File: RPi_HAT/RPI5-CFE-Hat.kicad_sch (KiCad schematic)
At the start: 64 parts, among them J1 Conn_01x16_Shielded, J2 SFP, J3 Bus_M.2_Socket_M, J5 Conn_02x03_Odd_Even, Q1 DMG1012T, Q2 DMG1012T, Q3 DMG1012T, U1 TPS564242DRLR, U2 PCA9306, U3 LM1117MP-1.8

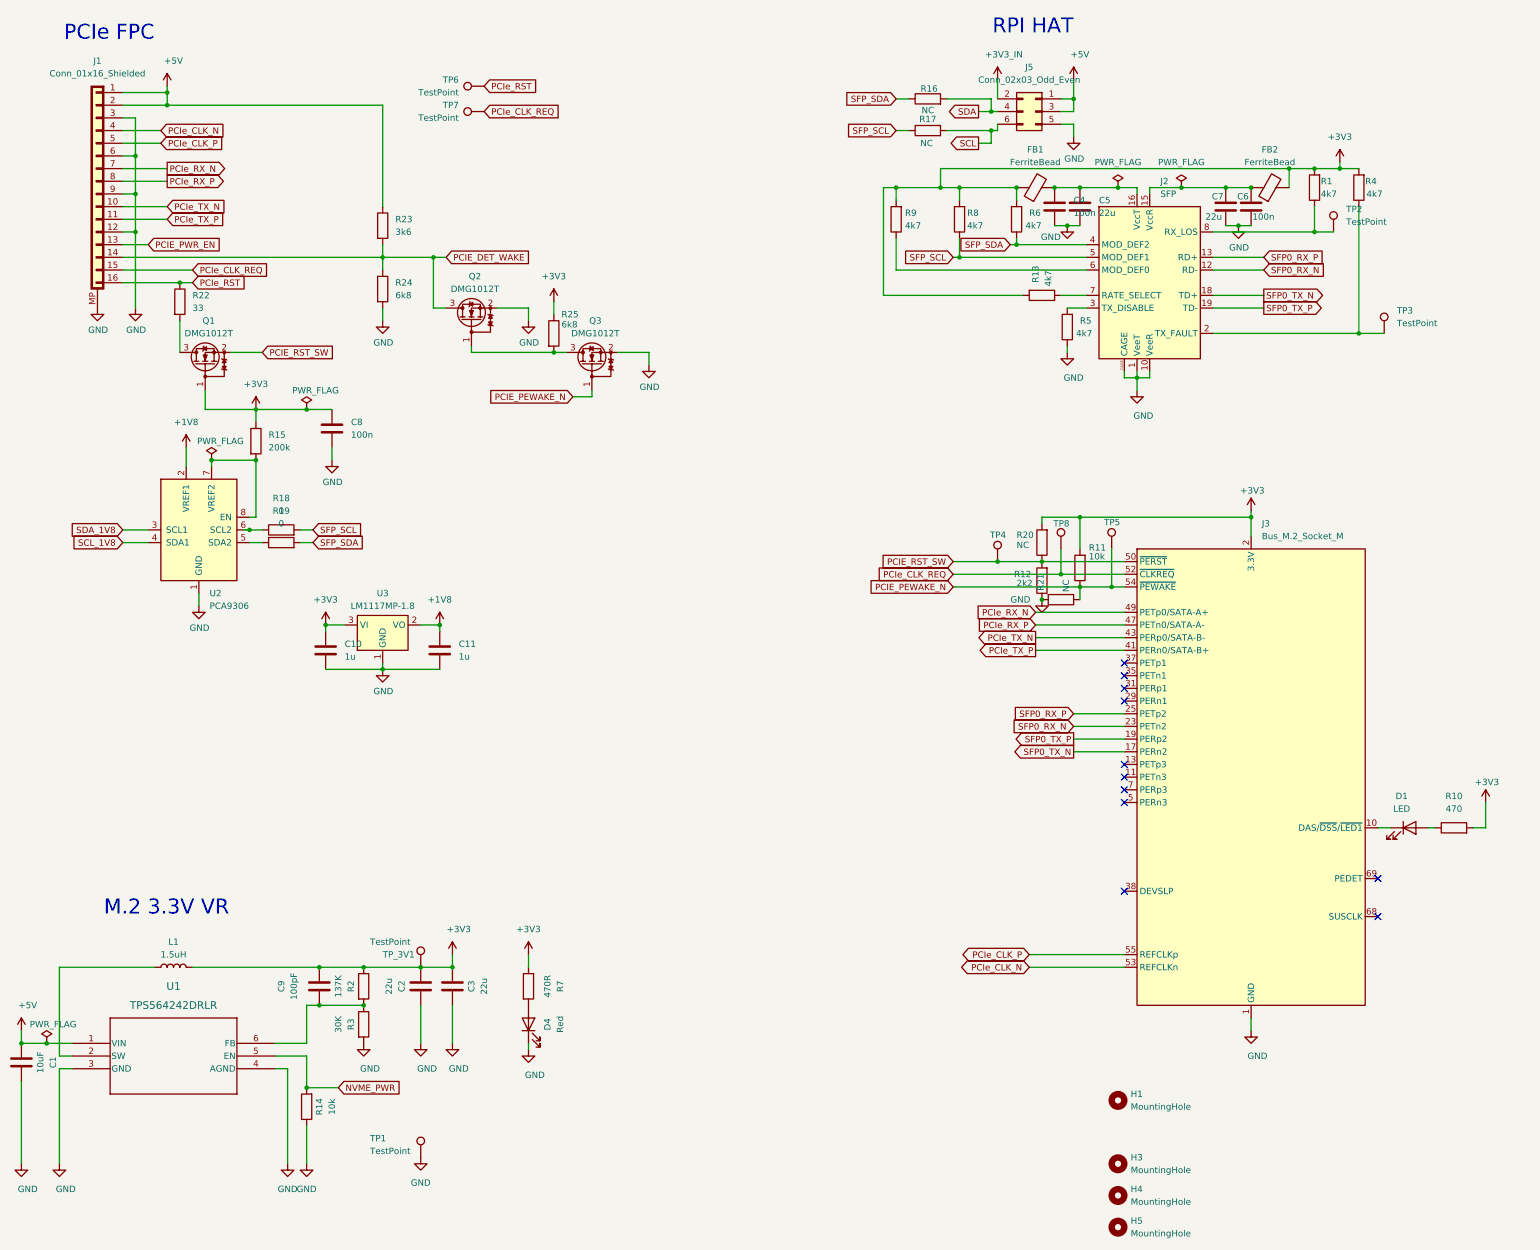
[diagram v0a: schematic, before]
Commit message: adjust differential pair skew
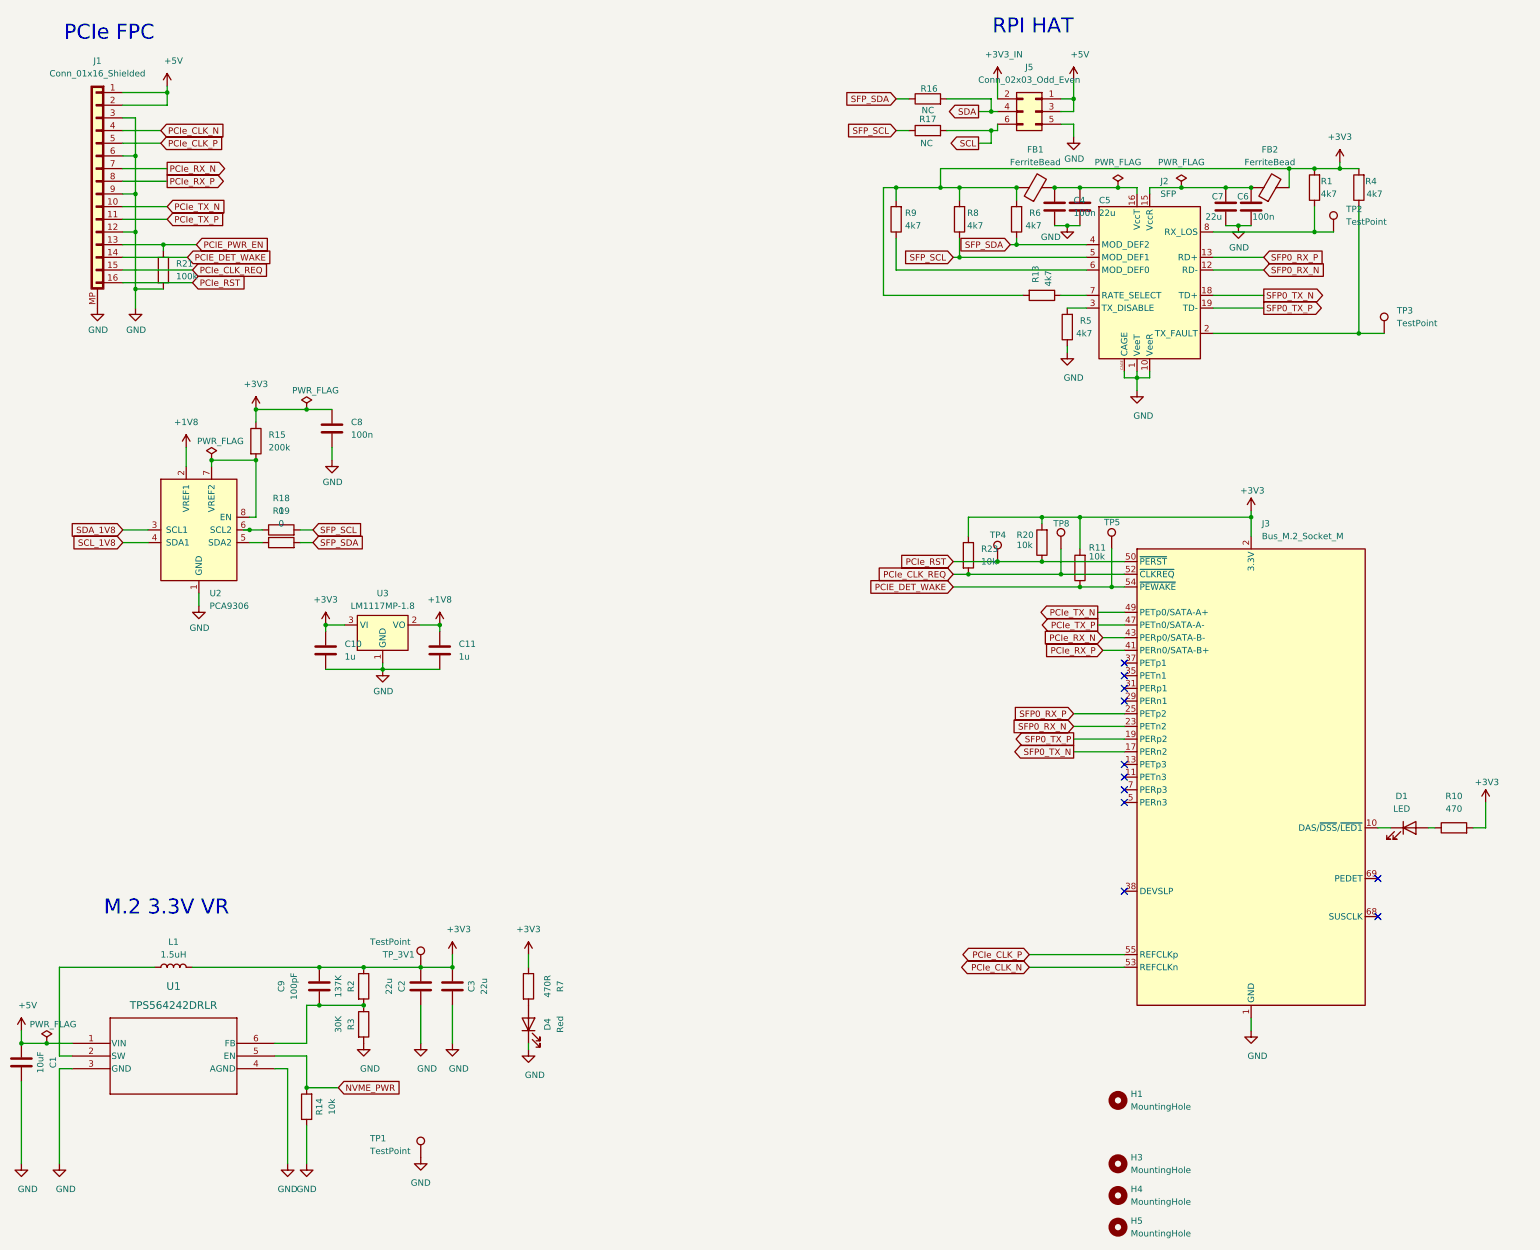
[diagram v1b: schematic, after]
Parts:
- removed Q1, Q2, Q3: DMG1012T, Package_TO_SOT_SMD:SOT-523, symbol Transistor_FET:DMG1012T
- removed R12: 2k2, Resistor_SMD:R_0402_1005Metric_Pad0.72x0.64mm_HandSolder, symbol Device:R
- removed R22: 33, Resistor_SMD:R_0402_1005Metric_Pad0.72x0.64mm_HandSolder, symbol Device:R
- removed R24, R25: 6k8, Resistor_SMD:R_0402_1005Metric_Pad0.72x0.64mm_HandSolder, symbol Device:R
- removed TP6, TP7: TestPoint, TestPoint:TestPoint_Pad_D1.0mm, symbol Connector:TestPoint
- R20: value NC -> 10k
- R21: value NC -> 100k
- R23: value 3k6 -> 10k
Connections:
- net PCIE_RST_SW is gone; now on net PCIe_RST: J3.50 (~{PERST}), R20.1, TP4.1
- net +3V3: now also R23.1
- net +5V: no longer R23.1
- net PCIE_DET_WAKE: now also J3.54 (~{PEWAKE}), R11.1, TP5.1; no longer R23.2
- net PCIE_PWR_EN: now also R21.1
- net PCIe_CLK_REQ: now also R23.2
- net PCIe_RX_N: now also J3.43 (PERp0/SATA-B-); no longer J3.49 (PETp0/SATA-A+)
- net PCIe_RX_P: now also J3.41 (PERn0/SATA-B+); no longer J3.47 (PETn0/SATA-A-)
- net PCIe_TX_N: now also J3.49 (PETp0/SATA-A+); no longer J3.43 (PERp0/SATA-B-)
- net PCIe_TX_P: now also J3.47 (PETn0/SATA-A-); no longer J3.41 (PERn0/SATA-B+)
- removed net PCIE_PEWAKE_N: J3.54 (~{PEWAKE}), R11.1, R21.1, TP5.1

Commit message: update board
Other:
- company: Will Whang -> JM Friedt
- title: RPI5-CFE-Hat -> RPI5-M2-SFP-Hat
- moved on the sheet: C1, C10, C11, C2, C3, C4, C5, C6, C7, C8, C9, D4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
